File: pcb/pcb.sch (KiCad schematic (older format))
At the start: 12 parts

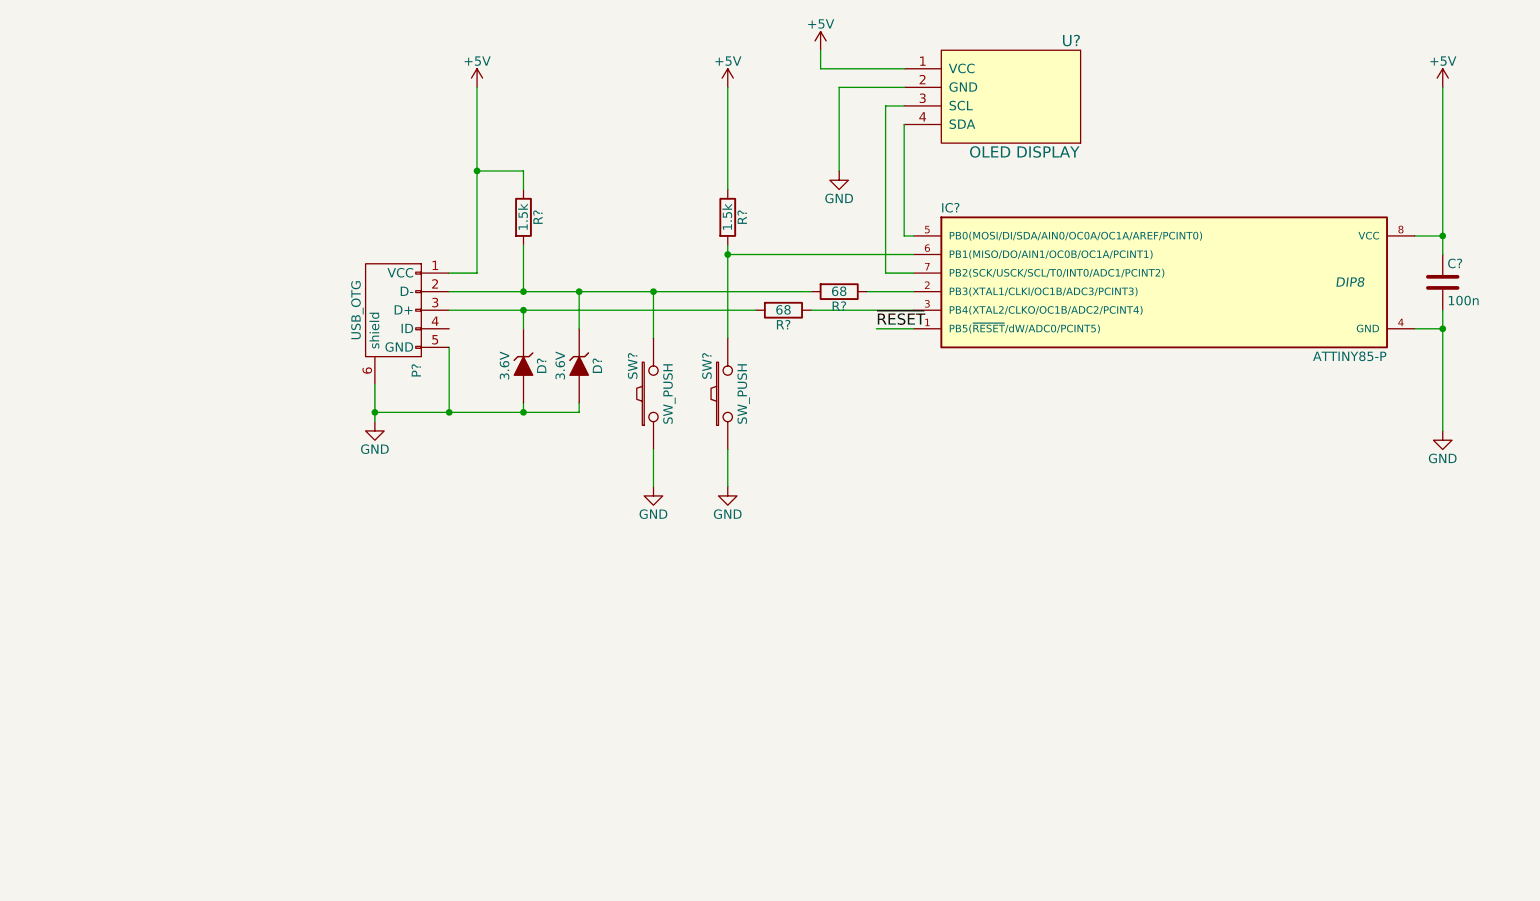
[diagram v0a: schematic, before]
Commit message: Modified button layout
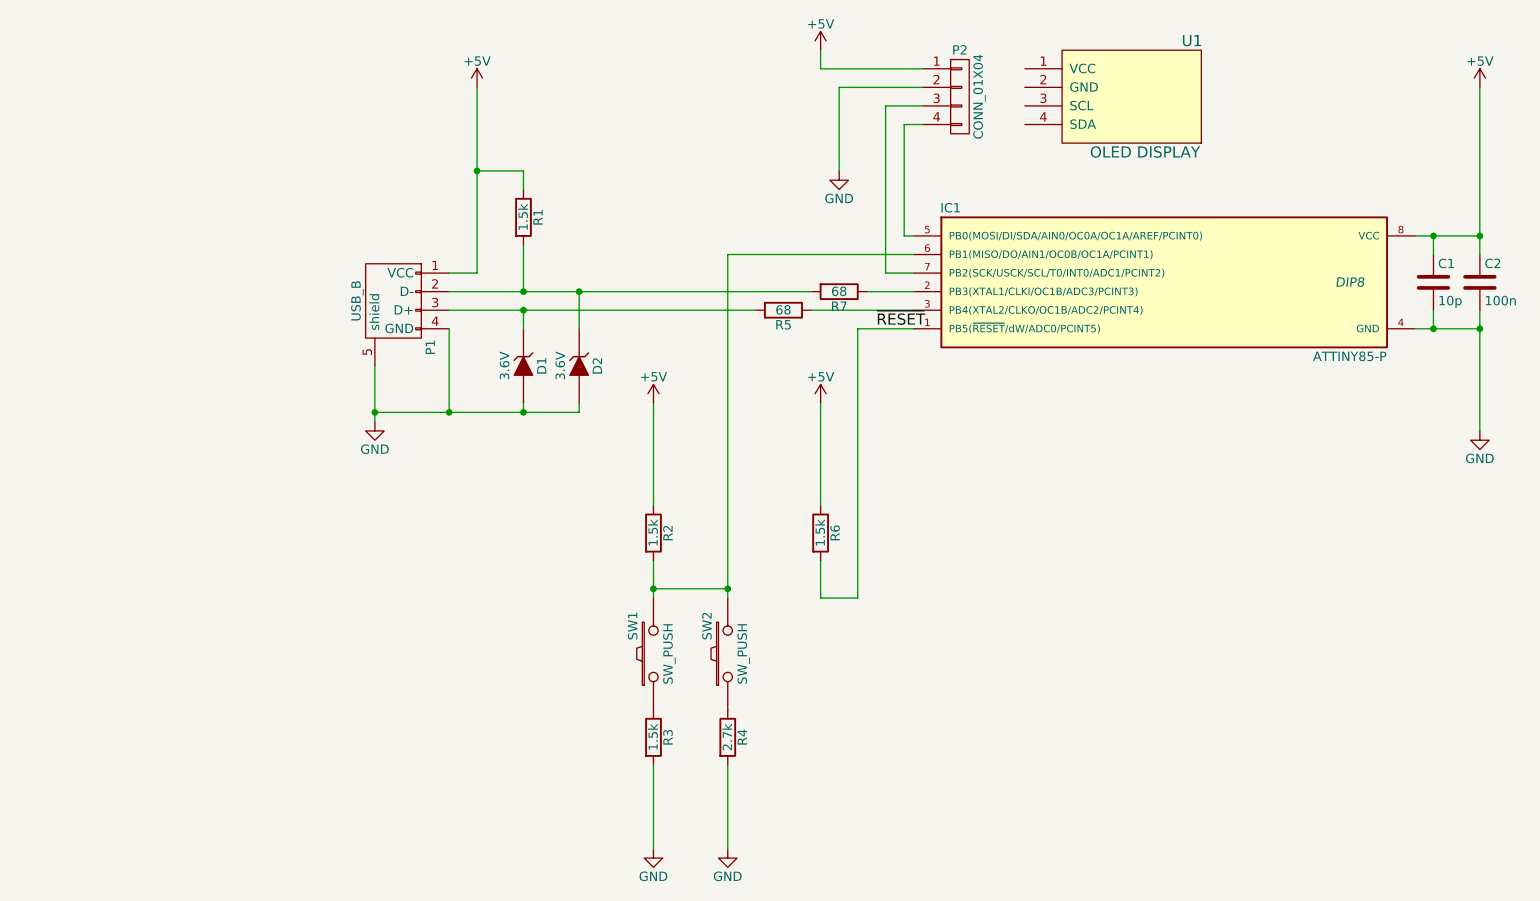
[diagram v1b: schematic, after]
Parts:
- removed P?: USB_OTG, symbol USB_OTG
- added C1: 10p, symbol C
- added P1: USB_B, symbol USB_B
- added P2: CONN_01X04, symbol CONN_01X04
- added R3, R6: 1.5k, symbol R
- added R4: 2.7k, symbol R
- gave numbers to parts that had none: 11
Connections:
- net +5V: now also C1.1, P1.1 (VCC), P2.1 (P1), R6.1; no longer U1.1 (VCC)
- net GND: now also C1.2, P1.4 (GND), P1.5 (shield), P2.2 (P2), R3.2, R4.2; no longer SW1.1, SW2.1, U1.2 (GND)
- net ~RESET: now also R6.2
- net at IC1.5 (PB0(MOSI/DI/SDA/AIN0/OC0A/OC1A/AREF/PCINT0)): now also P2.4 (P4); no longer U1.4 (SDA)
- net at IC1.6 (PB1(MISO/DO/AIN1/OC0B/OC1A/PCINT1)), R2.2, SW2.2: now also SW1.2
- net at IC1.7 (PB2(SCK/USCK/SCL/T0/INT0/ADC1/PCINT2)): now also P2.3 (P3); no longer U1.3 (SCL)
- net at D2.1 (K), R1.2, R7.2: now also P1.2 (D-); no longer SW1.2
- net at D1.1 (K), R5.2: now also P1.3 (D+)
- new net: R4.1, SW2.1
- new net: R3.1, SW1.1
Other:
- moved on the sheet: C2, R2, SW1, SW2, U1

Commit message: Removed warnings in Electrical Rules Checker
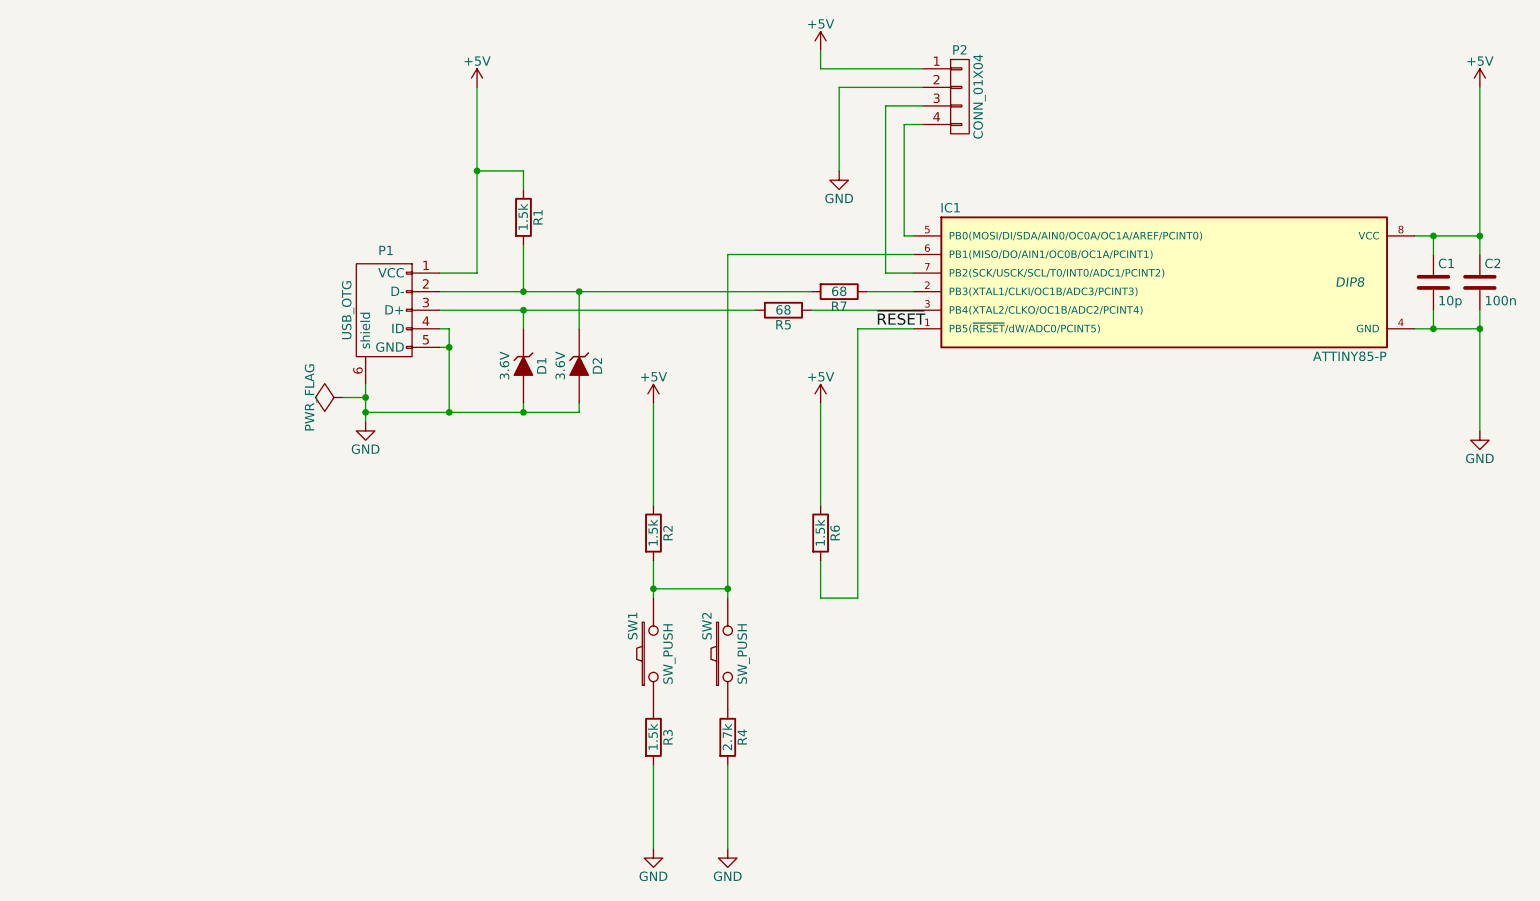
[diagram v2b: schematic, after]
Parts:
- removed P1: USB_B, symbol USB_B
- removed U1: OLED DISPLAY, symbol DISPLAY
- added P1: USB_OTG, symbol USB_OTG
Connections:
- net +5V: now also P1.1 (VCC)
- net GND: now also P1.4 (ID), P1.5 (GND), P1.6 (shield)
- net at D2.1 (K), R1.2, R7.2: now also P1.2 (D-)
- net at D1.1 (K), R5.2: now also P1.3 (D+)
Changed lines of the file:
@@
 $EndComp
 $Comp
-L +5V #PWR2
+L +5V #PWR01
 U 1 1 571FECFF
 P 3450 1250
-F 0 "#PWR2" H 3450 1100 50  0001 C CNN
+F 0 "#PWR01" H 3450 1100 50  0001 C CNN
 F 1 "+5V" H 3450 1390 50  0000 C CNN
 F 2 "" H 3450 1250 50  0000 C CNN
@@
 $EndComp
 $Comp
-L GND #PWR1
+L GND #PWR02
 U 1 1 571FED4A
-P 2900 3050
-F 0 "#PWR1" H 2900 2800 50  0001 C CNN
-F 1 "GND" H 2900 2900 50  0000 C CNN
-F 2 "" H 2900 3050 50  0000 C CNN
-F 3 "" H 2900 3050 50  0000 C CNN
-	1    2900 3050
+P 2850 3050
+F 0 "#PWR02" H 2850 2800 50  0001 C CNN
+F 1 "GND" H 2850 2900 50  0000 C CNN
+F 2 "" H 2850 3050 50  0000 C CNN
+F 3 "" H 2850 3050 50  0000 C CNN
+	1    2850 3050
 	1    0    0    -1
 $EndComp
@@
 $EndComp
 $Comp
-L GND #PWR10
+L GND #PWR03
 U 1 1 571FF958
 P 8850 3100
-F 0 "#PWR10" H 8850 2850 50  0001 C CNN
+F 0 "#PWR03" H 8850 2850 50  0001 C CNN
 F 1 "GND" H 8850 2950 50  0000 C CNN
 F 2 "" H 8850 3100 50  0000 C CNN
@@
 $EndComp
 $Comp
-L +5V #PWR9
+L +5V #PWR04
 U 1 1 571FF9A2
 P 8850 1250
-F 0 "#PWR9" H 8850 1100 50  0001 C CNN
+F 0 "#PWR04" H 8850 1100 50  0001 C CNN
 F 1 "+5V" H 8850 1390 50  0000 C CNN
 F 2 "" H 8850 1250 50  0000 C CNN
@@
 ~RESET
 $Comp
-L DISPLAY U1
-U 1 1 572002B9
-P 6950 1300
-F 0 "U1" H 6600 1600 60  0000 C CNN
-F 1 "OLED DISPLAY" H 7150 1000 60  0000 R CNN
-F 2 "" H 7950 750 60  0000 C CNN
-F 3 "" H 7950 750 60  0000 C CNN
-	1    6950 1300
-	-1   0    0    -1
-$EndComp
-$Comp
-L +5V #PWR6
+L +5V #PWR05
 U 1 1 5720046B
 P 5300 1050
-F 0 "#PWR6" H 5300 900 50  0001 C CNN
+F 0 "#PWR05" H 5300 900 50  0001 C CNN
 F 1 "+5V" H 5300 1190 50  0000 C CNN
 F 2 "" H 5300 1050 50  0000 C CNN
@@
 $EndComp
 $Comp
-L GND #PWR8
+L GND #PWR06
 U 1 1 57200491
 P 5400 1700
-F 0 "#PWR8" H 5400 1450 50  0001 C CNN
+F 0 "#PWR06" H 5400 1450 50  0001 C CNN
 F 1 "GND" H 5400 1550 50  0000 C CNN
 F 2 "" H 5400 1700 50  0000 C CNN
@@
 $EndComp
 $Comp
-L +5V #PWR3
+L +5V #PWR07
 U 1 1 572009AB
 P 4400 2950
-F 0 "#PWR3" H 4400 2800 50  0001 C CNN
+F 0 "#PWR07" H 4400 2800 50  0001 C CNN
 F 1 "+5V" H 4400 3090 50  0000 C CNN
 F 2 "" H 4400 2950 50  0000 C CNN
@@
 $EndComp
 $Comp
-L GND #PWR5
+L GND #PWR08
 U 1 1 57200ACD
 P 4800 5350
-F 0 "#PWR5" H 4800 5100 50  0001 C CNN
+F 0 "#PWR08" H 4800 5100 50  0001 C CNN
 F 1 "GND" H 4800 5200 50  0000 C CNN
 F 2 "" H 4800 5350 50  0000 C CNN
@@
 $EndComp
 $Comp
-L GND #PWR4
+L GND #PWR09
 U 1 1 57200AF7
 P 4400 5350
-F 0 "#PWR4" H 4400 5100 50  0001 C CNN
+F 0 "#PWR09" H 4400 5100 50  0001 C CNN
 F 1 "GND" H 4400 5200 50  0000 C CNN
 F 2 "" H 4400 5350 50  0000 C CNN
@@
 $EndComp
 $Comp
-L +5V #PWR7
+L +5V #PWR010
 U 1 1 572BD59D
 P 5300 2950
-F 0 "#PWR7" H 5300 2800 50  0001 C CNN
+F 0 "#PWR010" H 5300 2800 50  0001 C CNN
 F 1 "+5V" H 5300 3090 50  0000 C CNN
 F 2 "" H 5300 2950 50  0000 C CNN
@@
 	1    5300 2950
 	1    0    0    -1
-$EndComp
-$Comp
-L USB_B P1
-U 1 1 572BD8DA
-P 3000 2450
-F 0 "P1" H 3200 2250 50  0000 C CNN
-F 1 "USB_B" H 2950 2650 50  0000 C CNN
-F 2 "" V 2950 2350 50  0000 C CNN
-F 3 "" V 2950 2350 50  0000 C CNN
-	1    3000 2450
-	0    -1   1    0
 $EndComp
 $Comp
@@
 	1    0    0    -1
 $EndComp
+$Comp
+L USB_OTG P1
+U 1 1 5828F253
+P 2950 2450
+F 0 "P1" V 2630 2440 50  0000 C CNN
+F 1 "USB_OTG" H 2950 2650 50  0000 C CNN
+F 2 "" V 2900 2350 50  0000 C CNN
+F 3 "" V 2900 2350 50  0000 C CNN
+	1    2950 2450
+	0    -1   1    0
+$EndComp
 Wire Wire Line
 	5300 3500 5300 2950
@@
 Wire Wire Line
 	8850 2450 8850 3100
-Connection ~ 3700 3000
 Wire Wire Line
 	3700 2950 3700 3000
-Connection ~ 3300 3000
 Wire Wire Line
 	4000 3000 4000 2950
@@
 	3700 2550 3700 2450
 Wire Wire Line
-	3300 2450 4950 2450
-Wire Wire Line
-	3300 2350 5250 2350
+	3250 2450 4950 2450
+Wire Wire Line
+	3250 2350 5250 2350
 Connection ~ 3450 1700
 Wire Wire Line
@@
 Wire Wire Line
 	5800 2350 5550 2350
-Connection ~ 2900 3000
-Wire Wire Line
-	2900 3000 4000 3000
 Wire Wire Line
 	3300 2550 3300 3000
 Wire Wire Line
-	2900 2750 2900 3050
-Wire Wire Line
-	3450 1250 3450 2250
-Wire Wire Line
-	3450 2250 3300 2250
+	3450 2250 3450 1250
+Wire Wire Line
+	3250 2250 3450 2250
 Wire Wire Line
 	8500 2050 8850 2050
@@
 Wire Wire Line
 	5300 4000 5300 3800
+Wire Wire Line
+	2850 2850 2850 3050
+Wire Wire Line
+	2850 3000 4000 3000
+Connection ~ 3700 3000
+Connection ~ 2850 3000
+Connection ~ 3300 3000
+Wire Wire Line
+	3300 2550 3250 2550
+Wire Wire Line
+	3250 2650 3300 2650
+Connection ~ 3300 2650
+$Comp
+L PWR_FLAG #FLG011
+U 1 1 58290950
+P 2730 2920
+F 0 "#FLG011" H 2730 3015 50  0001 C CNN
+F 1 "PWR_FLAG" H 2730 3100 50  0000 C CNN
+F 2 "" H 2730 2920 50  0000 C CNN
+F 3 "" H 2730 2920 50  0000 C CNN
+	1    2730 2920
+	0    -1   -1   0
+$EndComp
+Wire Wire Line
+	2730 2920 2850 2920
+Connection ~ 2850 2920
 $EndSCHEMATC

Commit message: Created board layout in Pcbnew
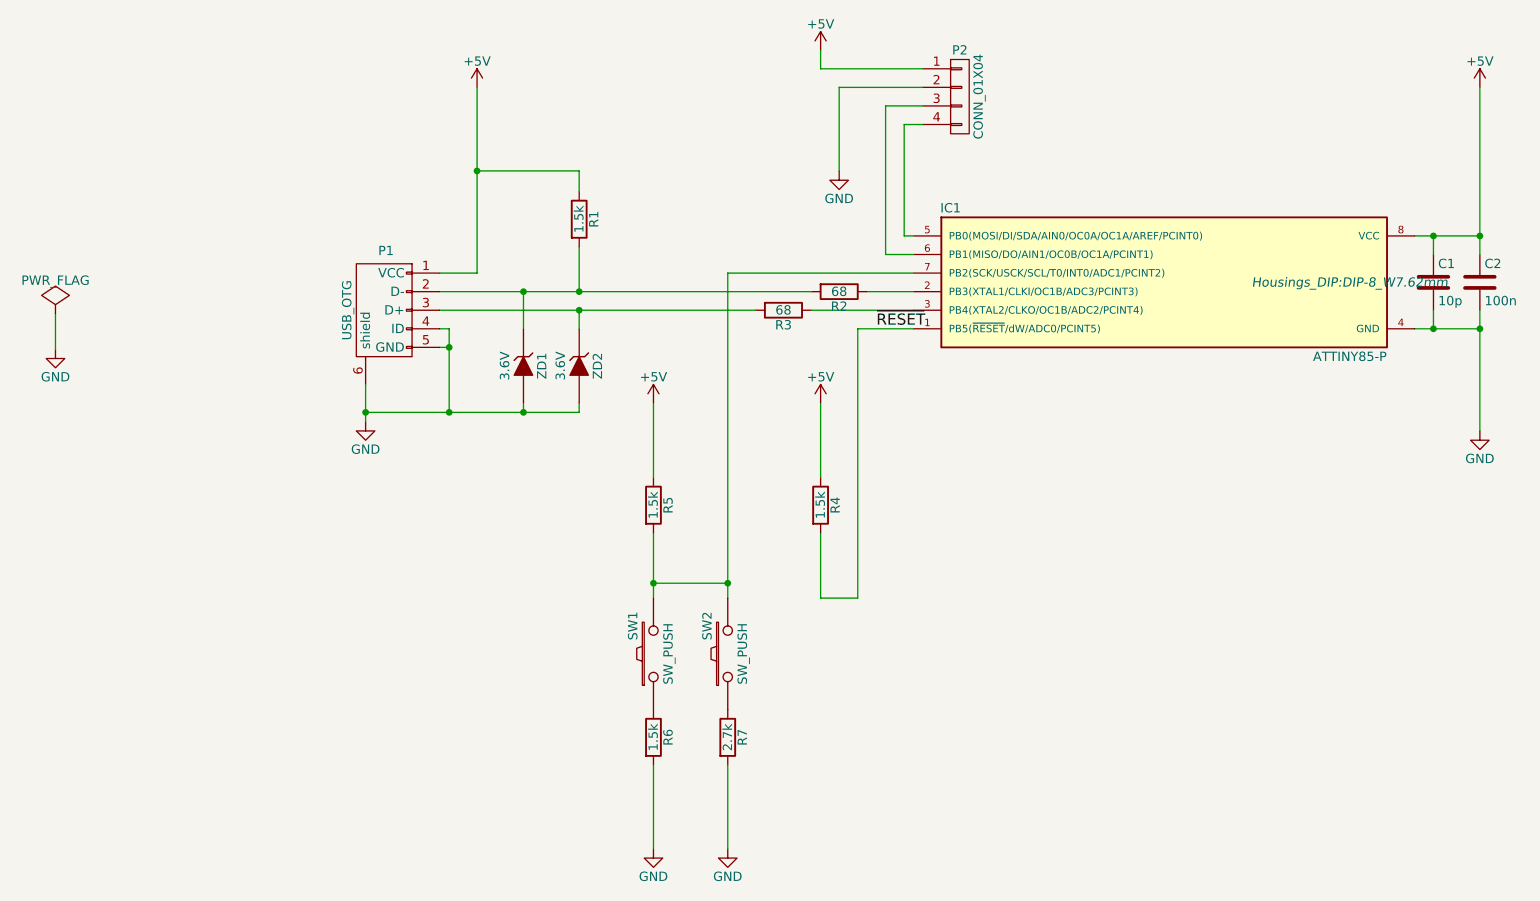
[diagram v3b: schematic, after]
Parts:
- C1, C2: footprint (none) -> Capacitors_SMD:C_1206_HandSoldering
- IC1: footprint DIP8 -> Housings_DIP:DIP-8_W7.62mm
- P1: footprint (none) -> Connect:USB_Micro-B
- P2: footprint (none) -> Socket_Strips:Socket_Strip_Straight_1x04
- R1: footprint (none) -> Resistors_SMD:R_1206_HandSoldering
- R2: renamed from R7; footprint (none) -> Resistors_SMD:R_1206_HandSoldering
- R3: renamed from R5; footprint (none) -> Resistors_SMD:R_1206_HandSoldering
- R4: renamed from R6; footprint (none) -> Resistors_SMD:R_1206_HandSoldering
- R5: renamed from R2; footprint (none) -> Resistors_SMD:R_1206_HandSoldering
- R6: renamed from R3; footprint (none) -> Resistors_SMD:R_1206_HandSoldering
- R7: renamed from R4; footprint (none) -> Resistors_SMD:R_1206_HandSoldering
- SW1, SW2: footprint (none) -> Buttons_Switches_SMD:SW_SPST_FSMSM
- ZD1: renamed from D1; footprint (none) -> Diodes_SMD:SOD-123
- ZD2: renamed from D2; footprint (none) -> Diodes_SMD:SOD-123
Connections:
- net at R5.2, SW1.2, SW2.2: now also IC1.7 (PB2(SCK/USCK/SCL/T0/INT0/ADC1/PCINT2)); no longer IC1.6 (PB1(MISO/DO/AIN1/OC0B/OC1A/PCINT1))
- net at P2.3 (P3): now also IC1.6 (PB1(MISO/DO/AIN1/OC0B/OC1A/PCINT1)); no longer IC1.7 (PB2(SCK/USCK/SCL/T0/INT0/ADC1/PCINT2))
- net at P1.2 (D-), R1.2, R2.2: now also ZD1.1 (K); no longer ZD2.1 (K)
- net at P1.3 (D+), R3.2: now also ZD2.1 (K); no longer ZD1.1 (K)
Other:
- moved on the sheet: R1, R4, R5
